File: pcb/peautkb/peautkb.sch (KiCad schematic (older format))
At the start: 184 parts, among them J1 Conn_01x04, J2 MJ-4PP-9, J3 Conn_01x04, J4 MJ-4PP-9, SW1 SW_PUSH, SW10 SW_PUSH, SW11 SW_PUSH, SW12 SW_PUSH, SW13 SW_PUSH, SW14 SW_PUSH, SW15 SW_PUSH, SW16 SW_PUSH, SW17 SW_PUSH, SW18 SW_PUSH, SW19 SW_PUSH, SW2 SW_PUSH, SW20 SW_PUSH, SW21 SW_PUSH, SW22 SW_PUSH, SW23 SW_PUSH, SW24 SW_PUSH, SW25 SW_PUSH, SW26 SW_PUSH, SW27 SW_PUSH, SW28 Rotary_Encoder_Switch, SW29 SW_PUSH, SW3 SW_PUSH, SW30 SW_PUSH, SW31 SW_PUSH, SW32 SW_PUSH, SW33 SW_PUSH, SW34 SW_PUSH, SW35 SW_PUSH, SW36 SW_PUSH, SW37 SW_PUSH, SW38 SW_PUSH, SW39 SW_PUSH, SW4 SW_PUSH, SW40 SW_PUSH, SW41 SW_PUSH, SW42 SW_PUSH, SW43 SW_PUSH, SW44 SW_PUSH, SW45 SW_PUSH, SW46 SW_PUSH, SW47 SW_PUSH, SW48 SW_PUSH, SW49 SW_PUSH, SW5 SW_PUSH, SW50 SW_PUSH, SW51 SW_PUSH, SW52 SW_PUSH, SW53 SW_PUSH, SW54 SW_PUSH, SW55 SW_PUSH, SW56 SW_PUSH, SW57 Rotary_Encoder_Switch, SW58 SW_PUSH, SW6 SW_PUSH, SW7 SW_PUSH, SW8 SW_PUSH, SW9 SW_PUSH, U1 black-pill-v3, U2 black-pill-v3

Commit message: removes extra col
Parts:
- removed D2, D3, D36, D37, D38, D4: D, kbd:D3_SMD_v2, symbol Device:D
- removed SW1, SW2, SW3, SW30, SW31, SW32: SW_PUSH, kbd:CherryMX_Hotswap, symbol kbd:SW_PUSH
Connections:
- net LCol6: now also SW22.1, SW23.1, SW24.1, SW25.1
- net RCol6: now also SW51.1, SW52.1, SW53.1, SW54.1
- net LCol0: no longer names the net of U1.33 (PA7)
- net RCol0: no longer names the net of U2.33 (PA7)
- no-connect marks 36 -> 38
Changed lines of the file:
@@
 $EndComp
 $Comp
-L kbd:SW_PUSH SW1
-U 1 1 605C75CC
-P 1270 1350
-F 0 "SW1" H 1270 1605 50  0000 C CNN
-F 1 "SW_PUSH" H 1270 1514 50  0000 C CNN
-F 2 "kbd:CherryMX_Hotswap" H 1270 1350 50  0001 C CNN
-F 3 "" H 1270 1350 50  0000 C CNN
-	1    1270 1350
-	1    0    0    -1
-$EndComp
-$Comp
 L kbd:SW_PUSH SW18
 U 1 1 605D1C8C
@@
 $EndComp
 $Comp
-L Device:D D2
-U 1 1 605FE8A8
-P 1570 1500
-F 0 "D2" V 1616 1420 50  0000 R CNN
-F 1 "D" V 1525 1420 50  0000 R CNN
-F 2 "kbd:D3_SMD_v2" H 1570 1500 50  0001 C CNN
-F 3 "~" H 1570 1500 50  0001 C CNN
-	1    1570 1500
-	0    -1   -1   0
-$EndComp
-$Comp
 L Device:D D6
 U 1 1 606015BC
@@
 	0    -1   -1   0
 $EndComp
-Text GLabel 970  950  1    50   Input ~ 0
-LCol0
-Wire Wire Line
-	1570 1650 2300 1650
 Wire Wire Line
 	2300 1650 3040 1650
-Connection ~ 2300 1650
 Wire Wire Line
 	3040 1650 3800 1650
@@
 $EndComp
 $Comp
-L kbd:SW_PUSH SW2
-U 1 1 6061D8B8
-P 1280 2000
-F 0 "SW2" H 1280 2255 50  0000 C CNN
-F 1 "SW_PUSH" H 1280 2164 50  0000 C CNN
-F 2 "kbd:CherryMX_Hotswap" H 1280 2000 50  0001 C CNN
-F 3 "" H 1280 2000 50  0000 C CNN
-	1    1280 2000
-	1    0    0    -1
-$EndComp
-$Comp
 L kbd:SW_PUSH SW19
 U 1 1 6061D8BE
@@
 $EndComp
 $Comp
-L Device:D D3
-U 1 1 6061D8D6
-P 1580 2150
-F 0 "D3" V 1626 2070 50  0000 R CNN
-F 1 "D" V 1535 2070 50  0000 R CNN
-F 2 "kbd:D3_SMD_v2" H 1580 2150 50  0001 C CNN
-F 3 "~" H 1580 2150 50  0001 C CNN
-	1    1580 2150
-	0    -1   -1   0
-$EndComp
-$Comp
 L Device:D D7
 U 1 1 6061D8DC
@@
 $EndComp
 $Comp
-L kbd:SW_PUSH SW3
-U 1 1 60628839
-P 1320 2710
-F 0 "SW3" H 1320 2965 50  0000 C CNN
-F 1 "SW_PUSH" H 1320 2874 50  0000 C CNN
-F 2 "kbd:CherryMX_Hotswap" H 1320 2710 50  0001 C CNN
-F 3 "" H 1320 2710 50  0000 C CNN
-	1    1320 2710
-	1    0    0    -1
-$EndComp
-$Comp
 L kbd:SW_PUSH SW21
 U 1 1 6062883F
@@
 $EndComp
 $Comp
-L Device:D D4
-U 1 1 60628857
-P 1620 2860
-F 0 "D4" V 1666 2780 50  0000 R CNN
-F 1 "D" V 1575 2780 50  0000 R CNN
-F 2 "kbd:D3_SMD_v2" H 1620 2860 50  0001 C CNN
-F 3 "~" H 1620 2860 50  0001 C CNN
-	1    1620 2860
-	0    -1   -1   0
-$EndComp
-$Comp
 L Device:D D8
 U 1 1 6062885D
@@
 $EndComp
 Wire Wire Line
-	970  2000 980  2000
-Wire Wire Line
-	970  950  970  1350
-Connection ~ 970  1350
-Wire Wire Line
-	970  1350 970  2000
-Wire Wire Line
-	980  2000 980  2710
-Wire Wire Line
-	980  2710 1020 2710
-Connection ~ 980  2000
-Wire Wire Line
 	1690 950  1690 1350
 Wire Wire Line
@@
 	4640 3540 4630 3540
 Wire Wire Line
-	5310 900  5310 1340
-Wire Wire Line
 	5300 1350 5310 1350
 Wire Wire Line
@@
 Wire Wire Line
 	5310 2000 5320 2000
-Connection ~ 5310 1350
 Wire Wire Line
 	5320 2000 5320 2710
@@
 Connection ~ 6810 1650
 Wire Wire Line
-	1580 2300 2310 2300
-Wire Wire Line
 	2310 2300 3050 2300
-Connection ~ 2310 2300
 Wire Wire Line
 	3050 2300 3810 2300
@@
 	6930 3010 6940 3010
 Wire Wire Line
-	1620 3010 2350 3010
-Wire Wire Line
 	2350 3010 3090 3010
-Connection ~ 2350 3010
 Wire Wire Line
 	3090 3010 3850 3010
@@
 $EndComp
 $Comp
-L kbd:SW_PUSH SW30
-U 1 1 6075B8D6
-P 9110 1370
-F 0 "SW30" H 9110 1625 50  0000 C CNN
-F 1 "SW_PUSH" H 9110 1534 50  0000 C CNN
-F 2 "kbd:CherryMX_Hotswap" H 9110 1370 50  0001 C CNN
-F 3 "" H 9110 1370 50  0000 C CNN
-	1    9110 1370
-	1    0    0    -1
-$EndComp
-$Comp
 L kbd:SW_PUSH SW47
 U 1 1 6075B8DC
@@
 $EndComp
 $Comp
-L Device:D D36
-U 1 1 6075B8F4
-P 9410 1520
-F 0 "D36" V 9456 1440 50  0000 R CNN
-F 1 "D" V 9365 1440 50  0000 R CNN
-F 2 "kbd:D3_SMD_v2" H 9410 1520 50  0001 C CNN
-F 3 "~" H 9410 1520 50  0001 C CNN
-	1    9410 1520
-	0    -1   -1   0
-$EndComp
-$Comp
 L Device:D D39
 U 1 1 6075B8FA
@@
 	0    -1   -1   0
 $EndComp
-Text GLabel 8810 970  1    50   Input ~ 0
-RCol0
-Wire Wire Line
-	9410 1670 10140 1670
 Wire Wire Line
 	10140 1670 10880 1670
-Connection ~ 10140 1670
 Wire Wire Line
 	10880 1670 11640 1670
@@
 $EndComp
 $Comp
-L kbd:SW_PUSH SW31
-U 1 1 6075B938
-P 9120 2020
-F 0 "SW31" H 9120 2275 50  0000 C CNN
-F 1 "SW_PUSH" H 9120 2184 50  0000 C CNN
-F 2 "kbd:CherryMX_Hotswap" H 9120 2020 50  0001 C CNN
-F 3 "" H 9120 2020 50  0000 C CNN
-	1    9120 2020
-	1    0    0    -1
-$EndComp
-$Comp
 L kbd:SW_PUSH SW48
 U 1 1 6075B93E
@@
 $EndComp
 $Comp
-L Device:D D37
-U 1 1 6075B956
-P 9420 2170
-F 0 "D37" V 9466 2090 50  0000 R CNN
-F 1 "D" V 9375 2090 50  0000 R CNN
-F 2 "kbd:D3_SMD_v2" H 9420 2170 50  0001 C CNN
-F 3 "~" H 9420 2170 50  0001 C CNN
-	1    9420 2170
-	0    -1   -1   0
-$EndComp
-$Comp
 L Device:D D40
 U 1 1 6075B95C
@@
 $EndComp
 $Comp
-L kbd:SW_PUSH SW32
-U 1 1 6075B98C
-P 9160 2730
-F 0 "SW32" H 9160 2985 50  0000 C CNN
-F 1 "SW_PUSH" H 9160 2894 50  0000 C CNN
-F 2 "kbd:CherryMX_Hotswap" H 9160 2730 50  0001 C CNN
-F 3 "" H 9160 2730 50  0000 C CNN
-	1    9160 2730
-	1    0    0    -1
-$EndComp
-$Comp
 L kbd:SW_PUSH SW50
 U 1 1 6075B992
@@
 $EndComp
 $Comp
-L Device:D D38
-U 1 1 6075B9AA
-P 9460 2880
-F 0 "D38" V 9506 2800 50  0000 R CNN
-F 1 "D" V 9415 2800 50  0000 R CNN
-F 2 "kbd:D3_SMD_v2" H 9460 2880 50  0001 C CNN
-F 3 "~" H 9460 2880 50  0001 C CNN
-	1    9460 2880
-	0    -1   -1   0
-$EndComp
-$Comp
 L Device:D D41
 U 1 1 6075B9B0
@@
 $EndComp
 Wire Wire Line
-	8810 2020 8820 2020
-Wire Wire Line
-	8810 970  8810 1370
-Connection ~ 8810 1370
-Wire Wire Line
-	8810 1370 8810 2020
-Wire Wire Line
-	8820 2020 8820 2730
-Wire Wire Line
-	8820 2730 8860 2730
-Connection ~ 8820 2020
-Wire Wire Line
 	9530 970  9530 1370
 Wire Wire Line
@@
 	12480 3560 12470 3560
 Wire Wire Line
-	13150 920  13150 1360
-Wire Wire Line
 	13140 1370 13150 1370
 Wire Wire Line
@@
 Wire Wire Line
 	13150 2020 13160 2020
-Connection ~ 13150 1370
 Wire Wire Line
 	13160 2020 13160 2730
@@
 Wire Wire Line
 	13170 3560 13160 3560
-Text GLabel 9530 970  1    50   Input ~ 0
-RCol1
 Text GLabel 10280 960  1    50   Input ~ 0
 RCol2
@@
 Connection ~ 14650 1670
 Wire Wire Line
-	9420 2320 10150 2320
-Wire Wire Line
 	10150 2320 10890 2320
-Connection ~ 10150 2320
 Wire Wire Line
 	10890 2320 11650 2320
@@
 	14770 3030 14780 3030
 Wire Wire Line
-	9460 3030 10190 3030
-Wire Wire Line
 	10190 3030 10930 3030
-Connection ~ 10190 3030
 Wire Wire Line
 	10930 3030 11690 3030
@@
 Text GLabel 4670 9775 2    50   Input ~ 0
 LSCA
-Text GLabel 3615 9410 2    50   Input ~ 0
-LCol0
 Text GLabel 3615 9515 2    50   Input ~ 0
 LCol1
@@
 LCol7
 Wire Wire Line
-	3255 9290 3570 9290
-Wire Wire Line
-	3570 9290 3570 9405
-Wire Wire Line
-	3570 9405 3615 9405
-Wire Wire Line
-	3615 9405 3615 9410
-Wire Wire Line
 	3255 9365 3555 9365
 Wire Wire Line
@@
 Text GLabel 10440 9695 2    50   Input ~ 0
 RSCA
-Text GLabel 9385 9330 2    50   Input ~ 0
-RCol0
 Text GLabel 9385 9435 2    50   Input ~ 0
 RCol1
@@
 RCol7
 Wire Wire Line
-	9025 9210 9340 9210
-Wire Wire Line
-	9340 9210 9340 9325
-Wire Wire Line
-	9340 9325 9385 9325
-Wire Wire Line
-	9385 9325 9385 9330
-Wire Wire Line
 	9025 9285 9325 9285
 Wire Wire Line
@@
 Wire Wire Line
 	3480 9740 3480 10040
+Wire Wire Line
+	5300 1350 5300 900
+Wire Wire Line
+	5300 900  5310 900
+Wire Wire Line
+	13140 1370 13140 920
+Wire Wire Line
+	13140 920  13150 920
+Connection ~ 10190 3030
+Wire Wire Line
+	9460 3030 10190 3030
+Text GLabel 9530 970  1    50   Input ~ 0
+RCol1
+NoConn ~ 3255 9290
+NoConn ~ 9025 9210
 $EndSCHEMATC

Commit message: left side traces completed
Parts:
- D52, D53, D54, D55, D57, D58, D59, D60, D63, D64, D65, D66, D67, D68, D69, D70: footprint kbd:D3_SMD -> kbd:D3_SMD_v2
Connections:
- net LCol2: now also SW8.1, SW9.1
- net LLED_In: now also D18.2 (DIN); no longer LED23.4 (DIN)
- net LRow0: now also U1.37 (PB10); no longer U1.34 (PB0)
- net LRow1: now also U1.36 (PB2); no longer U1.35 (PB1)
- net LRow2: now also U1.35 (PB1); no longer U1.36 (PB2)
- net LRow3: now also U1.34 (PB0); no longer U1.37 (PB10)
- net RLED_In: now also D46.2 (DIN); no longer LED48.4 (DIN)
- net RRow0: now also U2.37 (PB10); no longer U2.34 (PB0)
- net RRow1: now also U2.36 (PB2); no longer U2.35 (PB1)
- net RRow2: now also U2.35 (PB1); no longer U2.36 (PB2)
- net RRow3: now also U2.34 (PB0); no longer U2.37 (PB10)
- net at D1.2 (DIN): now also LED7.2 (DOUT); no longer LED3.2 (DOUT)
- net at D1.4 (DOUT): now also LED4.4 (DIN); no longer D5.2 (DIN)
- net at D5.4 (DOUT): now also LED6.4 (DIN); no longer D9.2 (DIN)
- net at D9.4 (DOUT): now also LED11.4 (DIN); no longer D13.2 (DIN)
- net at D13.4 (DOUT): now also LED13.4 (DIN); no longer D18.2 (DIN)
- net at D18.4 (DOUT): now also LED23.4 (DIN); no longer D22.2 (DIN)
- net at LED23.2 (DOUT): now also LED19.4 (DIN); no longer LED24.4 (DIN)
- net at LED24.2 (DOUT): now also LED21.4 (DIN); no longer LED25.4 (DIN)
- net at LED25.2 (DOUT): now also D22.2 (DIN); no longer LED22.4 (DIN)
- net at LED22.2 (DOUT): now also LED25.4 (DIN); no longer LED21.4 (DIN)
- net at LED21.2 (DOUT): now also LED17.4 (DIN); no longer LED20.4 (DIN)
- net at LED20.2 (DOUT): now also LED24.4 (DIN); no longer LED19.4 (DIN)
- net at LED15.2 (DOUT): now also D9.2 (DIN); no longer LED16.4 (DIN)
- net at LED16.2 (DOUT): now also LED20.4 (DIN); no longer LED17.4 (DIN)
- net at LED17.2 (DOUT): now also D13.2 (DIN); no longer LED18.4 (DIN)
- net at LED18.2 (DOUT): now also LED22.4 (DIN); no longer LED14.4 (DIN)
- net at LED14.2 (DOUT): now also LED18.4 (DIN); no longer LED13.4 (DIN)
- net at LED13.2 (DOUT): now also LED9.4 (DIN); no longer LED12.4 (DIN)
- net at LED12.2 (DOUT): now also LED16.4 (DIN); no longer LED11.4 (DIN)
- net at LED8.4 (DIN): now also LED5.2 (DOUT); no longer LED7.2 (DOUT)
- net at LED8.2 (DOUT): now also LED12.4 (DIN); no longer LED9.4 (DIN)
- net at LED9.2 (DOUT): now also D5.2 (DIN); no longer LED10.4 (DIN)
- net at LED10.2 (DOUT): now also LED14.4 (DIN); no longer LED6.4 (DIN)
- net at LED6.2 (DOUT): now also LED3.4 (DIN); no longer LED5.4 (DIN)
- net at LED2.2 (DOUT): now also LED5.4 (DIN); no longer LED3.4 (DIN)
- net at LED48.2 (DOUT): now also LED44.4 (DIN); no longer LED49.4 (DIN)
- net at LED49.2 (DOUT): now also LED46.4 (DIN); no longer LED50.4 (DIN)
- net at LED50.2 (DOUT): now also D62.2 (DIN); no longer LED47.4 (DIN)
- net at LED47.2 (DOUT): now also LED50.4 (DIN); no longer LED46.4 (DIN)
- net at LED46.2 (DOUT): now also LED42.4 (DIN); no longer LED45.4 (DIN)
- net at LED45.2 (DOUT): now also LED49.4 (DIN); no longer LED44.4 (DIN)
- net at LED40.2 (DOUT): now also D42.2 (DIN); no longer LED41.4 (DIN)
- net at LED41.2 (DOUT): now also LED45.4 (DIN); no longer LED42.4 (DIN)
- net at LED42.2 (DOUT): now also D61.2 (DIN); no longer LED43.4 (DIN)
- net at LED43.2 (DOUT): now also LED47.4 (DIN); no longer LED39.4 (DIN)
- net at LED39.2 (DOUT): now also LED43.4 (DIN); no longer LED38.4 (DIN)
- net at LED38.2 (DOUT): now also LED34.4 (DIN); no longer LED37.4 (DIN)
- net at LED37.2 (DOUT): now also LED41.4 (DIN); no longer LED36.4 (DIN)
- net at LED32.2 (DOUT): now also D51.2 (DIN); no longer LED33.4 (DIN)
- net at LED33.2 (DOUT): now also LED37.4 (DIN); no longer LED34.4 (DIN)
- net at LED34.2 (DOUT): now also D56.2 (DIN); no longer LED35.4 (DIN)
- net at LED35.2 (DOUT): now also LED39.4 (DIN); no longer LED31.4 (DIN)
- net at LED31.2 (DOUT): now also LED28.4 (DIN); no longer LED30.4 (DIN)
- net at LED30.2 (DOUT): now also LED33.4 (DIN); no longer LED29.4 (DIN)
- net at LED27.2 (DOUT): now also LED30.4 (DIN); no longer LED28.4 (DIN)
- net at LED28.2 (DOUT): now also LED35.4 (DIN); no longer D42.2 (DIN)
- net at D42.4 (DOUT): now also LED36.4 (DIN); no longer D46.2 (DIN)
- net at D46.4 (DOUT): now also LED48.4 (DIN); no longer D51.2 (DIN)
- net at D51.4 (DOUT): now also LED29.4 (DIN); no longer D56.2 (DIN)
- net at D56.4 (DOUT): now also LED31.4 (DIN); no longer D61.2 (DIN)
- net at D61.4 (DOUT): now also LED38.4 (DIN); no longer D62.2 (DIN)
- new net: LED10.4 (DIN), LED3.2 (DOUT)
- no-connect marks 38 -> 40
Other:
- moved on the sheet: D1, D13, D18, D22, D42, D46, D5, D51, D56, D61, D62, D9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

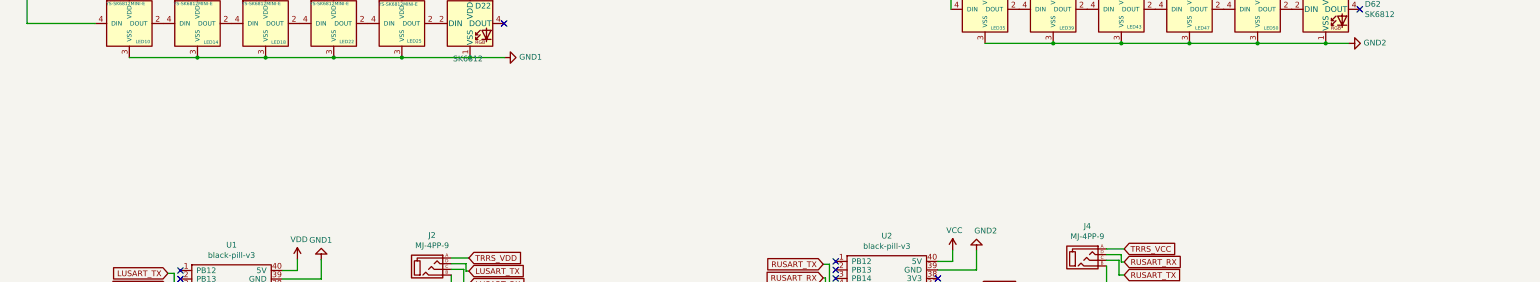
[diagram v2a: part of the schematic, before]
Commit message: aadded decoup caps to LHS
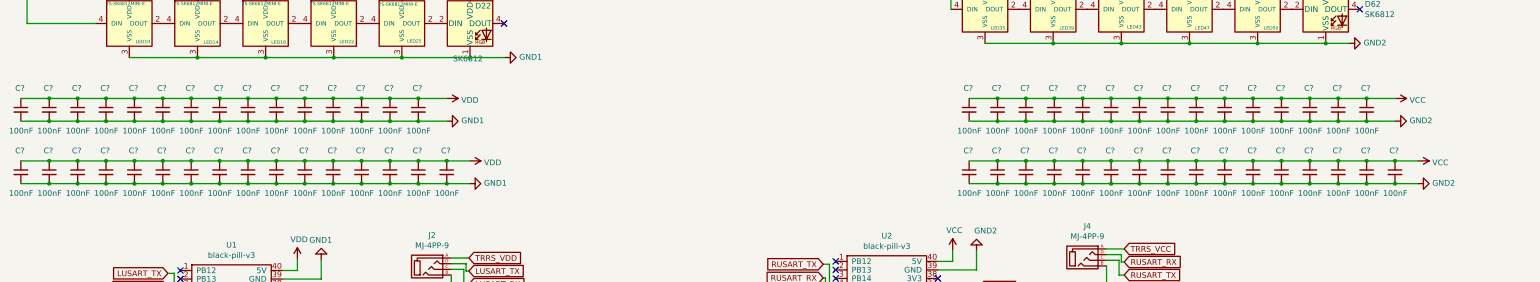
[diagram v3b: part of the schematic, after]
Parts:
- added C? (x62): 100nF, symbol Device:C_Small
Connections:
- net GND1: now also C?.2, C?.2, C?.2, C?.2, C?.2, C?.2, C?.2, C?.2, C?.2, C?.2, C?.2, C?.2, C?.2, C?.2, C?.2, C?.2, C?.2, C?.2, C?.2, C?.2, C?.2, C?.2, C?.2, C?.2, C?.2, C?.2, C?.2, C?.2, C?.2, C?.2, C?.2
- net GND2: now also C?.2, C?.2, C?.2, C?.2, C?.2, C?.2, C?.2, C?.2, C?.2, C?.2, C?.2, C?.2, C?.2, C?.2, C?.2, C?.2, C?.2, C?.2, C?.2, C?.2, C?.2, C?.2, C?.2, C?.2, C?.2, C?.2, C?.2, C?.2, C?.2, C?.2, C?.2
- net VCC: now also C?.1, C?.1, C?.1, C?.1, C?.1, C?.1, C?.1, C?.1, C?.1, C?.1, C?.1, C?.1, C?.1, C?.1, C?.1, C?.1, C?.1, C?.1, C?.1, C?.1, C?.1, C?.1, C?.1, C?.1, C?.1, C?.1, C?.1, C?.1, C?.1, C?.1, C?.1
- net VDD: now also C?.1, C?.1, C?.1, C?.1, C?.1, C?.1, C?.1, C?.1, C?.1, C?.1, C?.1, C?.1, C?.1, C?.1, C?.1, C?.1, C?.1, C?.1, C?.1, C?.1, C?.1, C?.1, C?.1, C?.1, C?.1, C?.1, C?.1, C?.1, C?.1, C?.1, C?.1
